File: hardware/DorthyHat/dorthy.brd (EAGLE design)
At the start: 100 x 100 mm, 28 parts, among them J1 90325-0004, J2 90325-0004, U1 DEV-15583

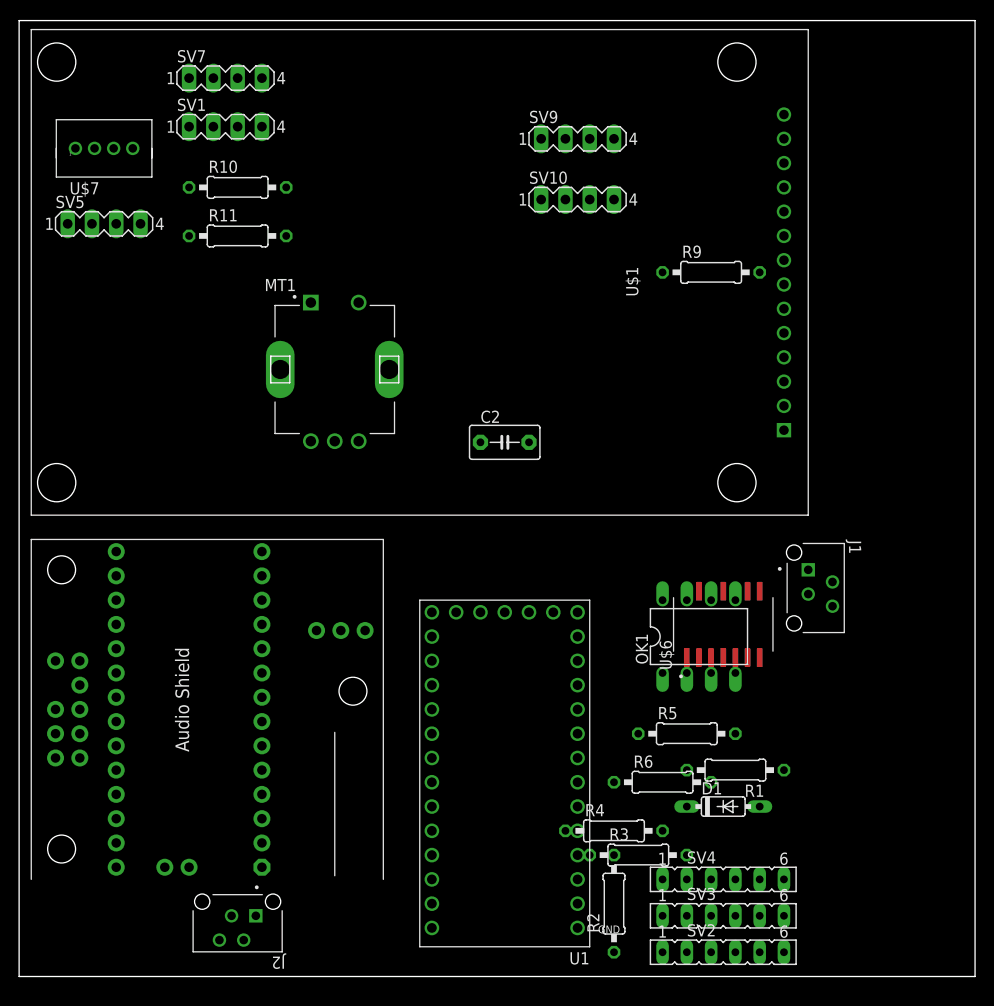
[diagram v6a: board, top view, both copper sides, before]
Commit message: Component placement first pass finished for Dorthy
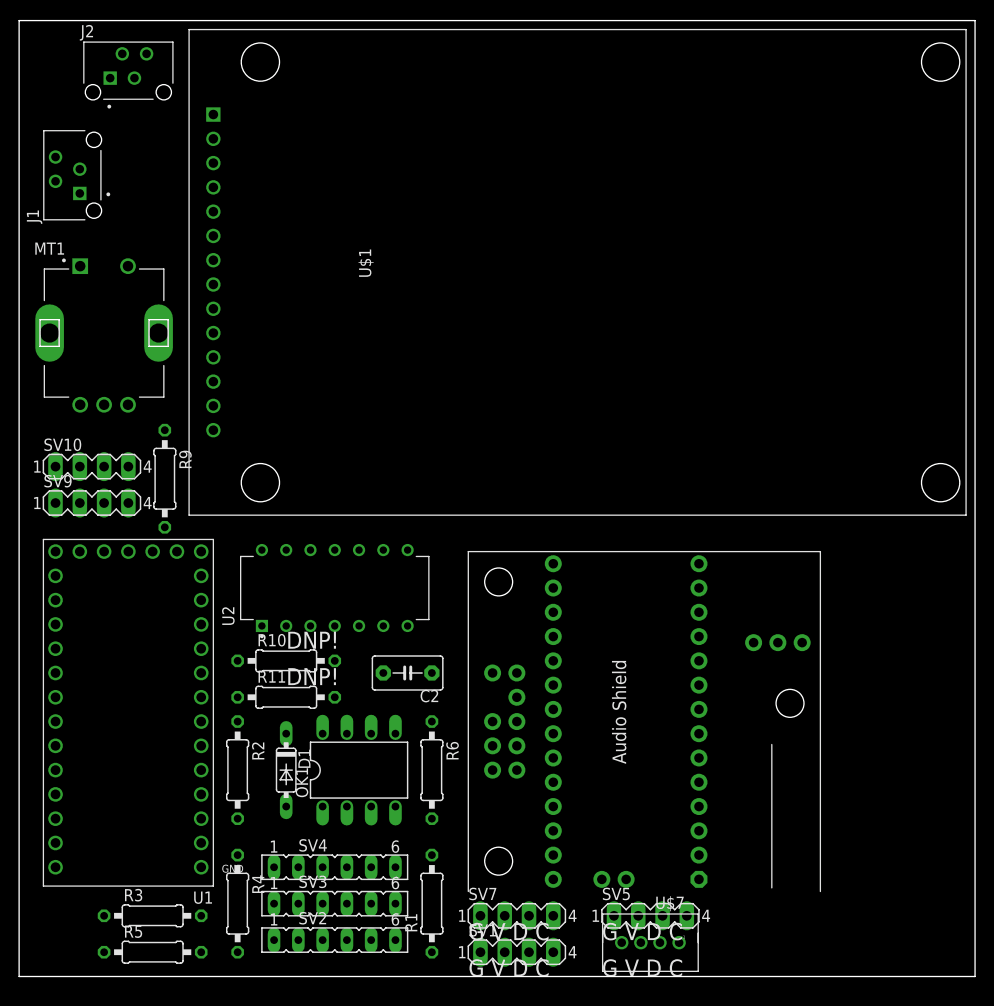
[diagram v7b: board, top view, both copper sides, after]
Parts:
- removed U$6: 74AHTC125NSR, DIP794W45P254L1969H508Q14:SOP127P780X200-14N
- added U2: SN74AHC125N, SN74AHC125N:DIP794W45P254L1969H508Q14
- moved U$7 102.5 mm to (66.0, 2.54), turned to 180 degrees
- moved SV7 92.8 mm to (52.1, 6.35)
- moved SV5 92.2 mm to (66.0, 6.35)
- moved SV1 91.6 mm to (52.1, 2.54)
- moved J2 90.9 mm to (11.4, 95.2), turned to 0 degrees
- moved J1 89.8 mm to (5.08, 83.8), turned to 90 degrees
- moved U$1 68.2 mm to (20.3, 90.2), turned to 270 degrees
- moved SV9 63.5 mm to (7.62, 49.5)
- moved R9 61.1 mm to (15.2, 52.1), turned to 270 degrees
- moved R5 60.4 mm to (14.0, 2.54)
- moved SV10 58.0 mm to (7.62, 53.3)
- moved R3 51.2 mm to (14.0, 6.35)
- moved R10 49.8 mm to (27.9, 33.0)
- moved R11 48.5 mm to (27.9, 29.2)
- moved D1 45.9 mm to (27.9, 21.6), turned to 270 degrees
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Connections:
- net GND: now also U2.1, U2.10, U2.13, U2.4, U2.7; no longer U$6.1, U$6.10, U$6.13, U$6.4, U$6.7
- net MIDIRX: now also U2.2; no longer U$6.2
- net MIDITX: now also U2.5; no longer U$6.5
- net O3A: now also U2.9; no longer U$6.9
- net O3Y: now also U2.8; no longer U$6.8
- net O4A: now also U2.12; no longer U$6.12
- net O4Y: now also U2.11; no longer U$6.11
- net RXBUF: now also U2.3; no longer U$6.3
- net TXBUF: now also U2.6; no longer U$6.6
- net VCC: now also U2.14; no longer U$6.14
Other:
- board text added: "DNP!"
- board text added: "G V D C"

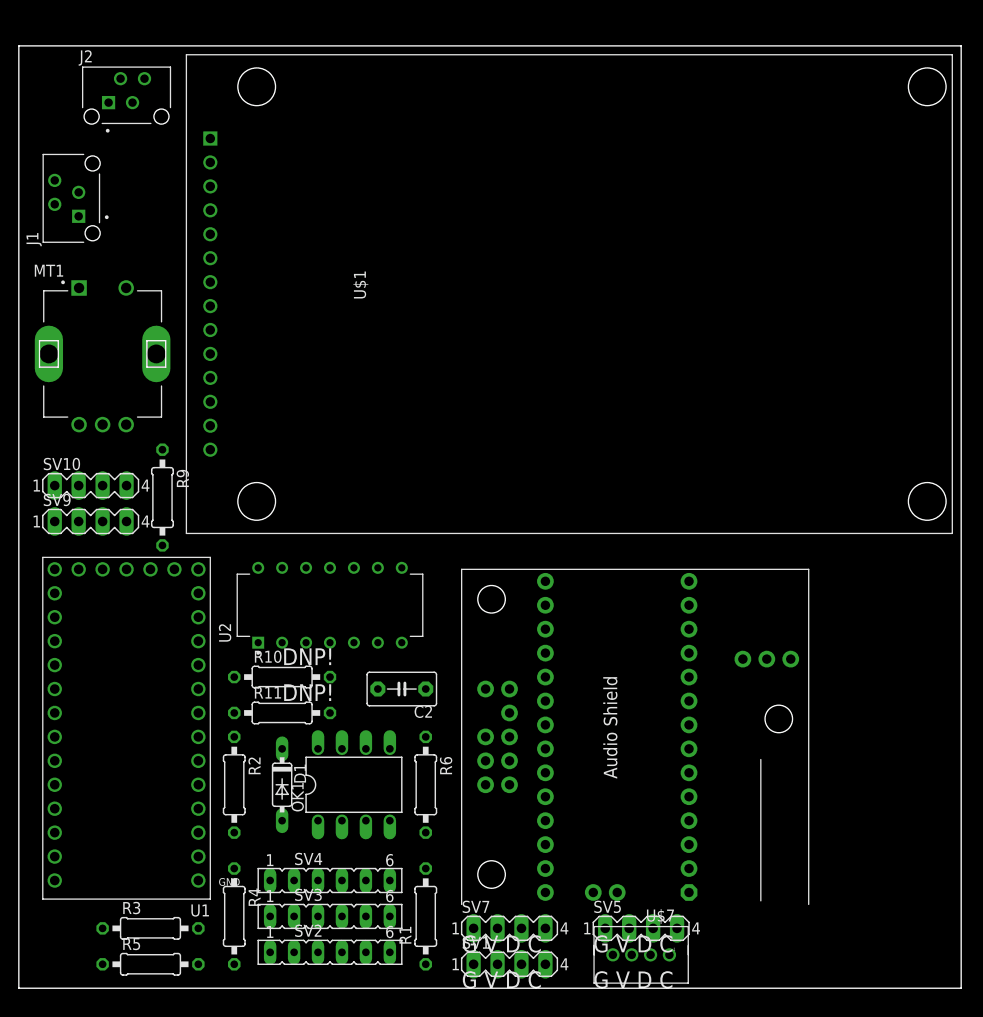
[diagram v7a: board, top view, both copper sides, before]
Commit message: add holes and polygons
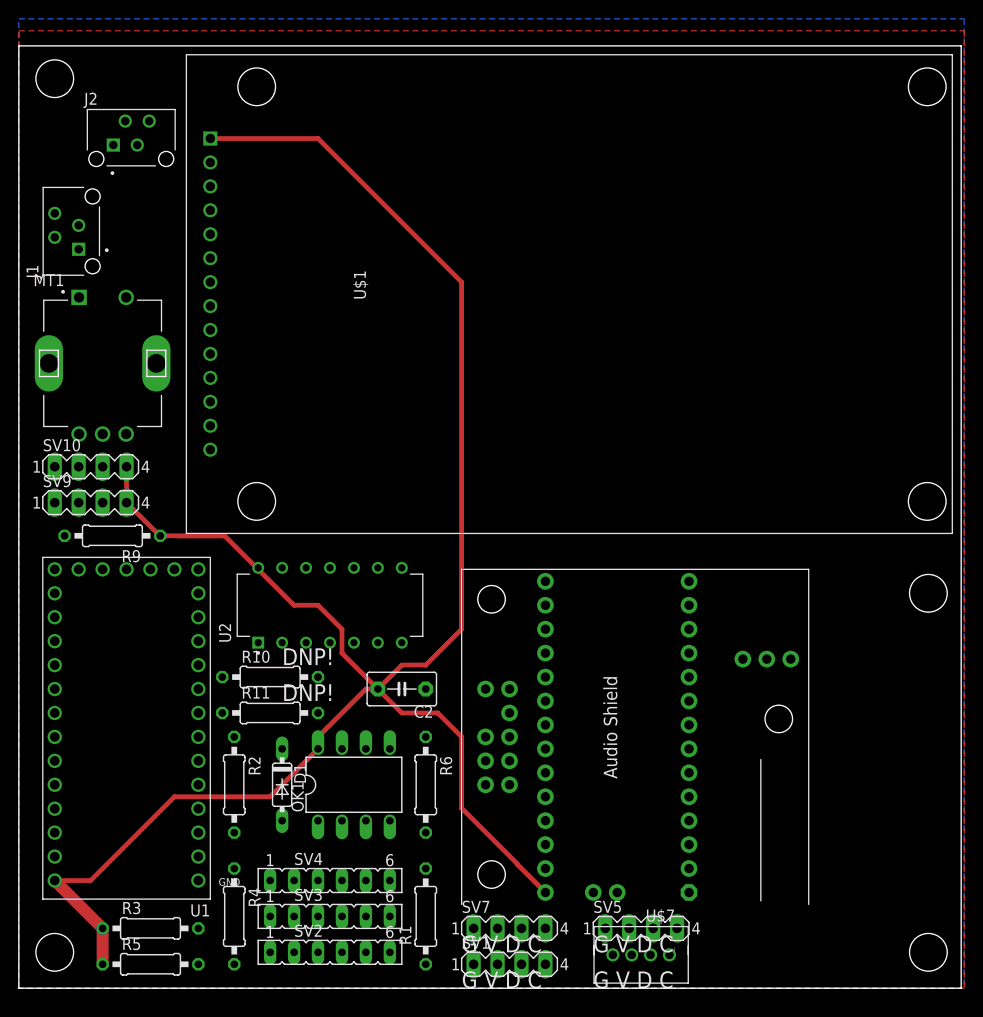
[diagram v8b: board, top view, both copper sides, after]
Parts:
- moved R9 6.68 mm to (9.93, 48.0), turned to 180 degrees
- moved J2 4.53 mm to (11.9, 90.8)
- moved J1 3.50 mm to (5.08, 80.3)
- moved SV10 2.00 mm to (7.62, 55.3)
- moved SV9 2.00 mm to (7.62, 51.5)
- moved R10 1.27 mm to (26.7, 33.0)
- moved R11 1.27 mm to (26.7, 29.2)
- moved MT1 1.00 mm to (8.89, 66.3)
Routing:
- net VCC: track 0.00 -> 207.2 mm
- added copper zone on layer 16, net GND
- added copper zone on layer 1, net VEE
